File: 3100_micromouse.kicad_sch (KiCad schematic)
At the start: 23 parts, among them J1 MOTOR1, J11 Extra +5V, J12 Extra +5V, J2 MOTOR2, J3 Extra GPIO A, J4 Extra GPIO B, J5 2 Pin PWR, J6 Aux SPI Bus, J7 Aux I2C Bus, J8 Extra Analog Pins, J9 UART Interface

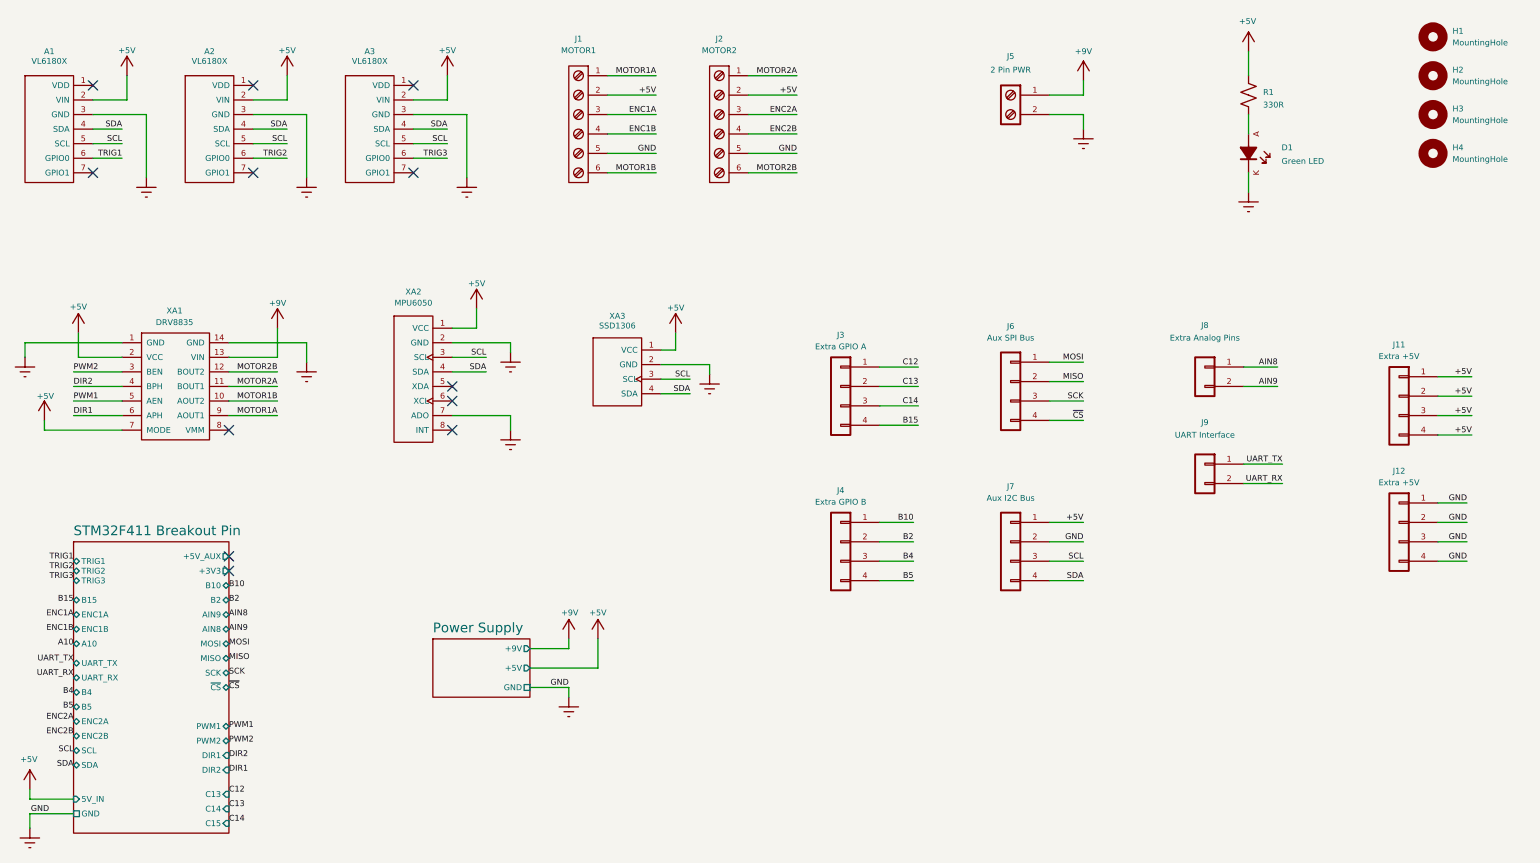
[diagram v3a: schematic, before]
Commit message: Finialized and Finished PCB routing
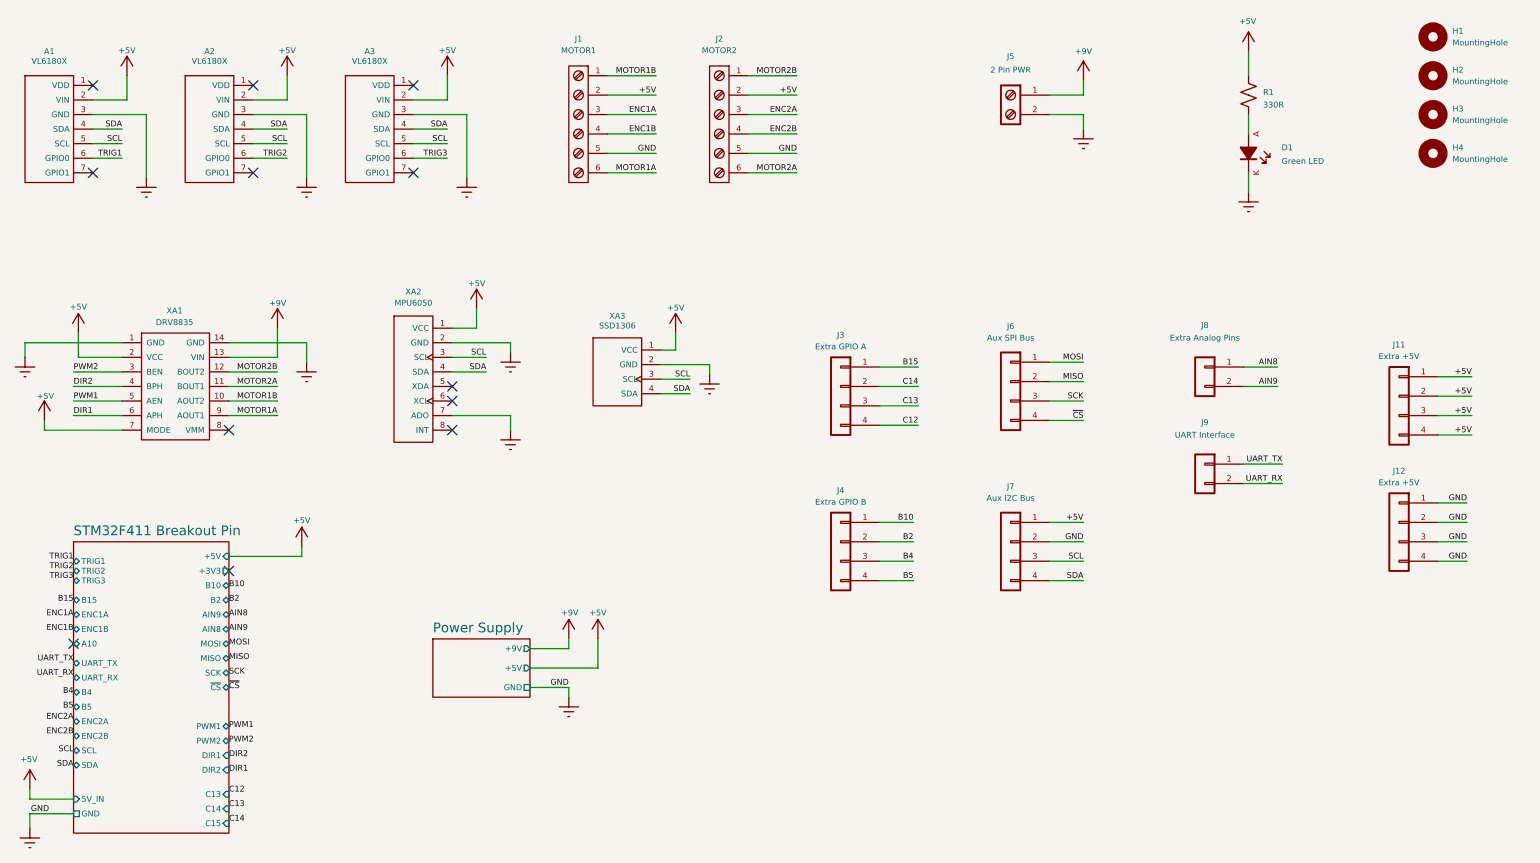
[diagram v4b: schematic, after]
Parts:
- H1, H2, H3, H4: footprint MountingHole:MountingHole_3.2mm_M3 -> MountingHole:MountingHole_3.2mm_M3_DIN965_Pad
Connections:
- net B15: now also J3.1 (Pin_1); no longer J3.4 (Pin_4)
- net C12: now also J3.4 (Pin_4); no longer J3.1 (Pin_1)
- net C13: now also J3.3 (Pin_3); no longer J3.2 (Pin_2)
- net C14: now also J3.2 (Pin_2); no longer J3.3 (Pin_3)
- net MOTOR1A: now also J1.6 (Pin_6); no longer J1.1 (Pin_1)
- net MOTOR1B: now also J1.1 (Pin_1); no longer J1.6 (Pin_6)
- net MOTOR2A: now also J2.6 (Pin_6); no longer J2.1 (Pin_1)
- net MOTOR2B: now also J2.1 (Pin_1); no longer J2.6 (Pin_6)
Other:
- sheet STM32F411 Breakout Pin ports: added +5V; removed +5V_AUX
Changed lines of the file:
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@@
 	)
 	(no_connect
-		(at 48.26 89.535)
-	)
-	(no_connect
 		(at 72.39 27.94)
 	)
@@
 	)
 	(no_connect
+		(at 27.94 100.965)
+	)
+	(no_connect
 		(at 51.435 39.37)
 	)
@@
 	(wire
 		(pts
+			(xy 57.785 89.535) (xy 57.785 88.265)
+		)
+		(stroke
+			(width 0)
+			(type default)
+		)
+	)
+	(wire
+		(pts
 			(xy 72.39 35.56) (xy 76.835 35.56)
 		)
@@
 	(wire
 		(pts
+			(xy 48.26 89.535) (xy 57.785 89.535)
+		)
+		(stroke
+			(width 0)
+			(type default)
+		)
+	)
+	(wire
+		(pts
 			(xy 181.61 31.75) (xy 181.61 34.29)
 		)
@@
 	)
 	(label "C14"
-		(at 138.43 69.85 180)
+		(at 138.43 67.31 180)
 		(effects
 			(font
@@
 	)
 	(label "MOTOR2A"
-		(at 122.555 26.67 180)
+		(at 122.555 39.37 180)
 		(effects
 			(font
@@
 	)
 	(label "MOTOR2B"
-		(at 122.555 39.37 180)
+		(at 122.555 26.67 180)
 		(effects
 			(font
@@
 	)
 	(label "C13"
-		(at 138.43 67.31 180)
+		(at 138.43 69.85 180)
 		(effects
 			(font
@@
 	)
 	(label "MOTOR1A"
-		(at 104.14 26.67 180)
+		(at 104.14 39.37 180)
 		(effects
 			(font
@@
 		)
 	)
-	(label "A10"
-		(at 27.94 100.965 180)
-		(effects
-			(font
-				(size 0.762 0.762)
-			)
-			(justify right)
-		)
-	)
 	(label "SDA"
 		(at 108.585 68.2625 180)
@@
 	)
 	(label "MOTOR1B"
-		(at 104.14 39.37 180)
+		(at 104.14 26.67 180)
 		(effects
 			(font
@@
 	)
 	(label "C12"
-		(at 138.43 64.77 180)
+		(at 138.43 72.39 180)
 		(effects
 			(font
@@
 	)
 	(label "B15"
-		(at 138.43 72.39 180)
+		(at 138.43 64.77 180)
 		(effects
 			(font
@@
 	)
 	(symbol
+		(lib_id "Power:VCC")
+		(at 57.785 88.265 0)
+		(unit 1)
+		(exclude_from_sim no)
+		(in_bom yes)
+		(on_board yes)
+		(dnp no)
+		(property "Reference" "#PWR032"
+			(at 57.785 92.075 0)
+			(effects
+				(font
+					(size 1.27 1.27)
+				)
+				(hide yes)
+			)
+		)
+		(property "Value" "+5V"
+			(at 57.785 84.836 0)
+			(effects
+				(font
+					(size 0.762 0.762)
+				)
+			)
+		)
+		(property "Footprint" ""
+			(at 57.785 88.265 0)
+			(effects
+				(font
+					(size 1.27 1.27)
+				)
+				(hide yes)
+			)
+		)
+		(property "Datasheet" ""
+			(at 57.785 88.265 0)
+			(effects
+				(font
+					(size 1.27 1.27)
+				)
+				(hide yes)
+			)
+		)
+		(property "Description" "Power symbol creates a global label with name \"VCC\""
+			(at 57.785 88.265 0)
+			(effects
+				(font
+					(size 1.27 1.27)
+				)
+				(hide yes)
+			)
+		)
+		(pin "1"
+		)
+		(instances
+			(project "3100_micromouse"
+				(path "/889dc75f-4037-4ec4-8f3e-1caf8b450acc"
+					(reference "#PWR032")
+					(unit 1)
+				)
+			)
+		)
+	)
+	(symbol
 		(lib_id "Connector_Generic:Conn_01x04")
 		(at 150.495 87.63 0)
@@
 			)
 		)
-		(property "Footprint" "MountingHole:MountingHole_3.2mm_M3"
+		(property "Footprint" "MountingHole:MountingHole_3.2mm_M3_DIN965_Pad"
 			(at 205.74 31.75 0)
 			(effects
@@
 			)
 		)
-		(property "Footprint" "MountingHole:MountingHole_3.2mm_M3"
+		(property "Footprint" "MountingHole:MountingHole_3.2mm_M3_DIN965_Pad"
 			(at 205.74 26.67 0)
 			(effects
@@
 			)
 		)
-		(property "Footprint" "MountingHole:MountingHole_3.2mm_M3"
+		(property "Footprint" "MountingHole:MountingHole_3.2mm_M3_DIN965_Pad"
 			(at 205.74 36.83 0)
 			(effects
@@
 			)
 		)
-		(property "Footprint" "MountingHole:MountingHole_3.2mm_M3"
+		(property "Footprint" "MountingHole:MountingHole_3.2mm_M3_DIN965_Pad"
 			(at 205.74 21.59 0)
 			(effects
@@
 			)
 		)
-		(pin "+5V_AUX" output
-			(at 48.26 89.535 0)
-			(effects
-				(font
-					(size 0.762 0.762)
-				)
-				(justify right)
-			)
-		)
 		(pin "TRIG1" bidirectional
 			(at 27.94 90.17 180)
@@
 			)
 		)
+		(pin "+5V" input
+			(at 48.26 89.535 0)
+			(effects
+				(font
+					(size 0.762 0.762)
+				)
+				(justify right)
+			)
+		)
